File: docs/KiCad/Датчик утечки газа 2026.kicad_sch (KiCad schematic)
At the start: 30 parts, among them J1 Conn_01x04_Pin, J2 Conn_01x04_Pin, Q1 BC846BDW1, Q2 AO4807, U1 TGS_2611-E00, U2 LMR50410, U3 ATtiny412-SS

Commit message: Исправление разводки платы Ver_LIN
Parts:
- R2: footprint Resistor_SMD:R_1210_3225Metric_Pad1.30x2.65mm_HandSolder -> Resistor_SMD:R_1206_3216Metric
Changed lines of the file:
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@@
 			)
 		)
-		(property "Footprint" "Resistor_SMD:R_1210_3225Metric_Pad1.30x2.65mm_HandSolder"
+		(property "Footprint" "Resistor_SMD:R_1206_3216Metric"
 			(at 66.04 127.762 90)
 			(hide yes)

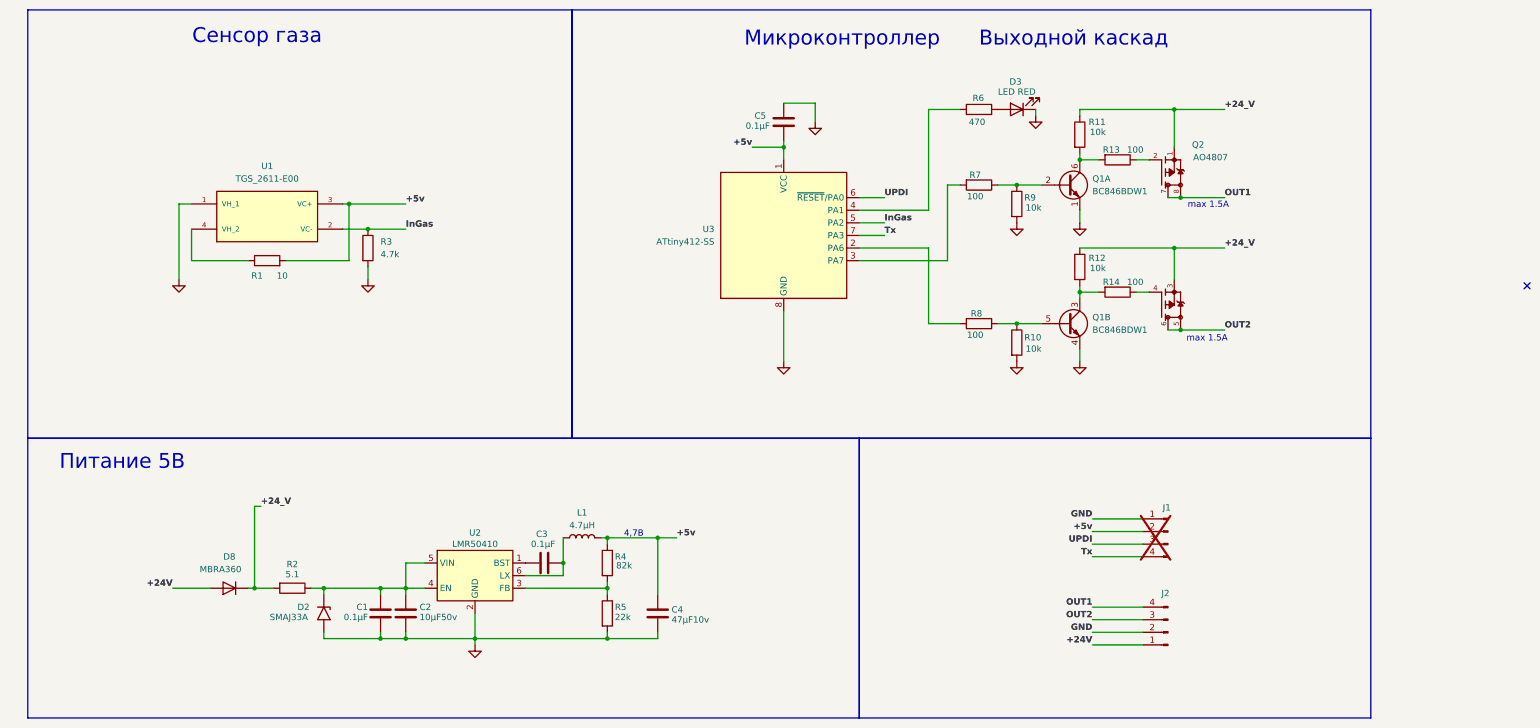
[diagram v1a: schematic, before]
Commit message: Изменить выходной ключ на умный. Правки печатной платы
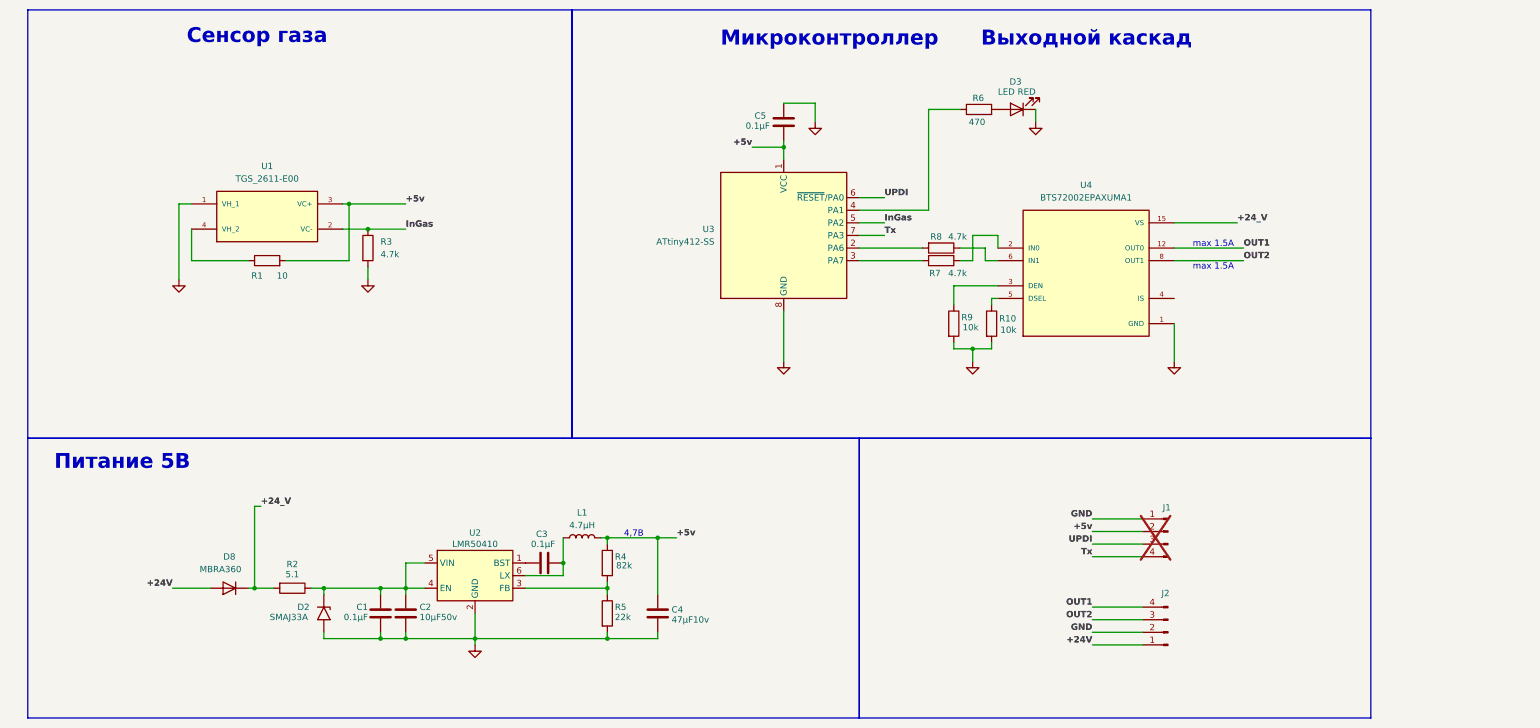
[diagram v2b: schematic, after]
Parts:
- removed Q1: BC846BDW1, Package_TO_SOT_SMD:SOT-363_SC-70-6, symbol Transistor_BJT:BC846BDW1
- removed Q2: AO4807, Package_SO:SOIC-8_3.9x4.9mm_P1.27mm, symbol AO4407A:AO4807
- removed R11, R12: 10k, Resistor_SMD:R_0603_1608Metric, symbol Device:R
- removed R13, R14: 100, Resistor_SMD:R_0603_1608Metric, symbol Device:R
- added U4: BTS72002EPAXUMA1, Package_TO_SOT_SMD:SOP65P600X115-15N_BTS72002EPAXUMA1, symbol Driver:BTS72002EPAXUMA1
- J2: footprint Connector_Pin:AMP SEAL 3.00mm_4p -> Connector_DIN:SSEAL_4
- R7, R8: value 100 -> 4.7k
- U1: footprint Sensor:TO180P920X780-4P -> Sensor_Humidity:TO180P920X780-4P
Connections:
- net +24_V: now also U4.15 (VS)
- net GND: now also U4.1 (GND)
- net OUT1: now also U4.12 (OUT0), U4.13 (OUT0), U4.14 (OUT0)
- net OUT2: now also U4.10 (OUT1), U4.8 (OUT1), U4.9 (OUT1)
- net at R7.1: now also U4.2 (IN0); no longer R9.1
- net at R10.1: now also U4.5 (DSEL); no longer R8.1
- new net: R9.1, U4.3 (DEN)
- new net: R8.1, U4.6 (IN1)
- no-connect marks 1 -> 0
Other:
- moved on the sheet: R10, R7, R8, R9

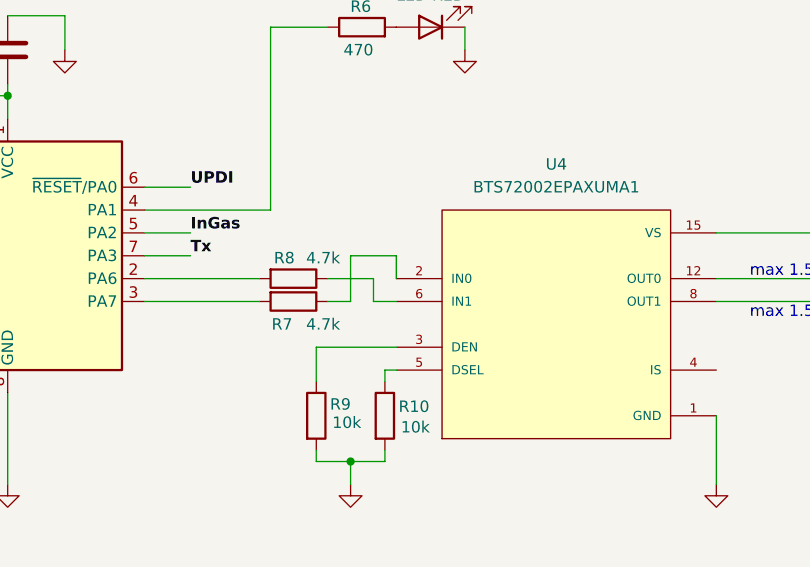
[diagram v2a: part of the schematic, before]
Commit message: Коррекция ПП. Замена выходной ключ на BTS72002
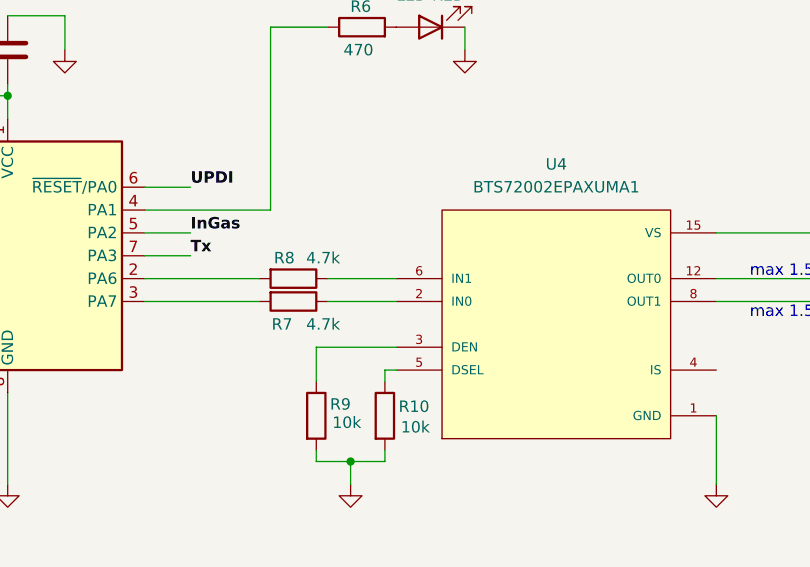
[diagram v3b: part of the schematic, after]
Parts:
- R2: footprint Resistor_SMD:R_1206_3216Metric -> Resistor_SMD:R_0805_2012Metric
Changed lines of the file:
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@@
 	(wire
 		(pts
-			(xy 208.28 58.42) (xy 208.28 60.96)
-		)
-		(stroke
-			(width 0)
-			(type default)
-		)
-	)
-	(wire
-		(pts
 			(xy 165.1 31.75) (xy 171.45 31.75)
 		)
@@
 	(wire
 		(pts
-			(xy 203.2 63.5) (xy 203.2 58.42)
-		)
-		(stroke
-			(width 0)
-			(type default)
-		)
-	)
-	(wire
-		(pts
 			(xy 207.01 71.12) (xy 208.28 71.12)
 		)
@@
 	(wire
 		(pts
-			(xy 205.74 63.5) (xy 208.28 63.5)
-		)
-		(stroke
-			(width 0)
-			(type default)
-		)
-	)
-	(wire
-		(pts
 			(xy 77.47 52.07) (xy 77.47 63.5)
 		)
@@
 	(wire
 		(pts
-			(xy 200.66 60.96) (xy 205.74 60.96)
+			(xy 200.66 60.96) (xy 208.28 60.96)
 		)
 		(stroke
@@
 	(wire
 		(pts
-			(xy 200.66 63.5) (xy 203.2 63.5)
+			(xy 200.66 63.5) (xy 208.28 63.5)
 		)
 		(stroke
@@
 	(wire
 		(pts
-			(xy 205.74 60.96) (xy 205.74 63.5)
-		)
-		(stroke
-			(width 0)
-			(type default)
-		)
-	)
-	(wire
-		(pts
 			(xy 227.33 135.89) (xy 237.49 135.89)
 		)
@@
 	(wire
 		(pts
-			(xy 203.2 58.42) (xy 208.28 58.42)
-		)
-		(stroke
-			(width 0)
-			(type default)
-		)
-	)
-	(wire
-		(pts
 			(xy 120.65 119.38) (xy 120.65 124.46)
 		)
@@
 			)
 		)
-		(property "Description" "AC0603KRX7R9BB104"
+		(property "Description" "Unpolarized capacitor"
 			(at 116.84 124.46 0)
 			(hide yes)
@@
 			)
 		)
-		(property "Description" "GRM21BR61A476ME15L"
+		(property "Description" "Unpolarized capacitor"
 			(at 139.7 134.62 0)
 			(hide yes)
@@
 			)
 		)
-		(property "Sim.Device" "MBRA360, Диод Шоттки 60В 3А [SMA / DO-214AC]"
+		(property "Sim.Device" "D"
 			(at 53.34 129.54 0)
 			(hide yes)
@@
 			)
 		)
-		(property "Description" "LQH44PN4R7MP0L"
+		(property "Description" "Inductor"
 			(at 124.46 119.38 0)
 			(hide yes)
@@
 			)
 		)
-		(property "Description" "FYLS-0805URC"
+		(property "Description" "Light emitting diode"
 			(at 212.09 33.02 0)
 			(hide yes)
@@
 			)
 		)
-		(property "Footprint" "Resistor_SMD:R_1206_3216Metric"
+		(property "Footprint" "Resistor_SMD:R_0805_2012Metric"
 			(at 66.04 127.762 90)
 			(hide yes)
@@
 			)
 		)
-		(property "Description" "AC0603KRX7R9BB104"
+		(property "Description" "Unpolarized capacitor"
 			(at 83.82 134.62 0)
 			(hide yes)
@@
 			)
 		)
-		(property "Description" "GRM21BR61H106KE43L"
+		(property "Description" "Unpolarized capacitor"
 			(at 88.9 134.62 0)
 			(hide yes)
@@
 			)
 		)
-		(property "Description" "AC0603KRX7R9BB104"
+		(property "Description" "Unpolarized capacitor"
 			(at 165.1 35.56 0)
 			(hide yes)

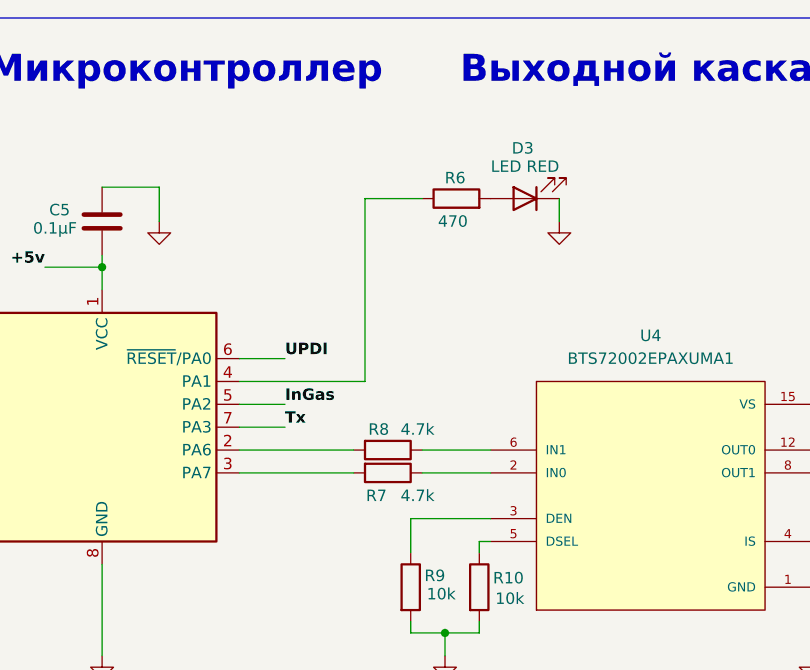
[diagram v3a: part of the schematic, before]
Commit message: Коррекция схемы для драйвера BTS72002EPAXUMA1
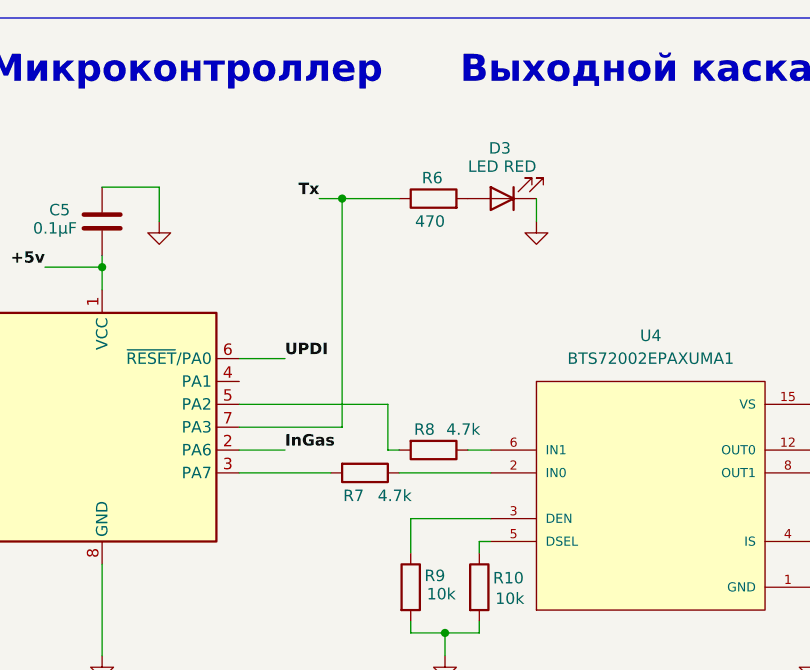
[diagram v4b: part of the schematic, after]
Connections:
- net InGas: now also U3.2 (PA6); no longer U3.5 (PA2)
- net Tx: now also R6.1
- net at R8.2: now also U3.5 (PA2); no longer U3.2 (PA6)
- net at U3.4 (PA1): no longer R6.1
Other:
- moved on the sheet: D3, R6, R7, R8
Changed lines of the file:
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@@
 	)
 	(junction
+		(at 191.77 33.02)
+		(diameter 0)
+		(color 0 0 0 0)
+	)
+	(junction
 		(at 83.82 139.7)
 		(diameter 0)
@@
 	(wire
 		(pts
-			(xy 194.31 33.02) (xy 200.66 33.02)
+			(xy 191.77 33.02) (xy 198.12 33.02)
 		)
 		(stroke
@@
 	(wire
 		(pts
-			(xy 180.34 55.88) (xy 185.42 55.88)
-		)
-		(stroke
-			(width 0)
-			(type default)
-		)
-	)
-	(wire
-		(pts
 			(xy 203.2 83.82) (xy 203.2 81.28)
 		)
@@
 	(wire
 		(pts
-			(xy 200.66 60.96) (xy 208.28 60.96)
+			(xy 205.74 60.96) (xy 208.28 60.96)
 		)
 		(stroke
@@
 	(wire
 		(pts
+			(xy 196.85 55.88) (xy 180.34 55.88)
+		)
+		(stroke
+			(width 0)
+			(type default)
+		)
+	)
+	(wire
+		(pts
 			(xy 207.01 72.39) (xy 207.01 71.12)
 		)
@@
 	(wire
 		(pts
-			(xy 200.66 63.5) (xy 208.28 63.5)
+			(xy 198.12 63.5) (xy 208.28 63.5)
 		)
 		(stroke
@@
 	(wire
 		(pts
-			(xy 180.34 58.42) (xy 185.42 58.42)
-		)
-		(stroke
-			(width 0)
-			(type default)
-		)
-	)
-	(wire
-		(pts
 			(xy 199.39 68.58) (xy 208.28 68.58)
 		)
@@
 	(wire
 		(pts
-			(xy 180.34 63.5) (xy 193.04 63.5)
+			(xy 180.34 63.5) (xy 190.5 63.5)
 		)
 		(stroke
@@
 	(wire
 		(pts
-			(xy 215.9 35.56) (xy 215.9 33.02)
+			(xy 213.36 35.56) (xy 213.36 33.02)
 		)
 		(stroke
@@
 	(wire
 		(pts
-			(xy 194.31 33.02) (xy 194.31 53.34)
+			(xy 180.34 58.42) (xy 191.77 58.42)
 		)
 		(stroke
@@
 	(wire
 		(pts
-			(xy 180.34 60.96) (xy 193.04 60.96)
+			(xy 191.77 33.02) (xy 191.77 58.42)
 		)
 		(stroke
@@
 	(wire
 		(pts
+			(xy 189.23 33.02) (xy 191.77 33.02)
+		)
+		(stroke
+			(width 0)
+			(type default)
+		)
+	)
+	(wire
+		(pts
 			(xy 207.01 81.28) (xy 207.01 80.01)
 		)
@@
 	(wire
 		(pts
+			(xy 196.85 60.96) (xy 196.85 55.88)
+		)
+		(stroke
+			(width 0)
+			(type default)
+		)
+	)
+	(wire
+		(pts
 			(xy 58.42 113.03) (xy 58.42 129.54)
 		)
@@
 	(wire
 		(pts
+			(xy 198.12 60.96) (xy 196.85 60.96)
+		)
+		(stroke
+			(width 0)
+			(type default)
+		)
+	)
+	(wire
+		(pts
 			(xy 64.77 63.5) (xy 77.47 63.5)
 		)
@@
 	(wire
 		(pts
-			(xy 81.28 67.31) (xy 81.28 64.77)
+			(xy 180.34 60.96) (xy 185.42 60.96)
 		)
 		(stroke
@@
 	(wire
 		(pts
-			(xy 129.54 139.7) (xy 129.54 138.43)
+			(xy 81.28 67.31) (xy 81.28 64.77)
 		)
 		(stroke
@@
 	(wire
 		(pts
-			(xy 57.15 129.54) (xy 58.42 129.54)
+			(xy 129.54 139.7) (xy 129.54 138.43)
 		)
 		(stroke
@@
 	(wire
 		(pts
-			(xy 77.47 52.07) (xy 88.9 52.07)
+			(xy 57.15 129.54) (xy 58.42 129.54)
 		)
 		(stroke
@@
 	(wire
 		(pts
-			(xy 194.31 53.34) (xy 180.34 53.34)
+			(xy 77.47 52.07) (xy 88.9 52.07)
 		)
 		(stroke
@@
 	)
 	(label "Tx"
-		(at 185.42 58.42 0)
-		(effects
-			(font
-				(size 1.27 1.27)
-				(thickness 0.254)
-				(bold yes)
-			)
-			(justify left bottom)
-		)
-	)
-	(label "Tx"
 		(at 227.33 123.19 180)
 		(effects
@@
 	)
 	(label "InGas"
-		(at 185.42 55.88 0)
+		(at 88.9 57.15 0)
 		(effects
 			(font
@@
 	)
 	(label "InGas"
-		(at 88.9 57.15 0)
+		(at 185.42 60.96 0)
 		(effects
 			(font
@@
 		)
 	)
+	(label "Tx"
+		(at 189.23 33.02 180)
+		(effects
+			(font
+				(size 1.27 1.27)
+				(thickness 0.254)
+				(bold yes)
+			)
+			(justify right bottom)
+		)
+	)
 	(label "OUT1"
 		(at 227.33 133.35 180)
@@
 	(symbol
 		(lib_id "Device:R")
-		(at 196.85 63.5 270)
+		(at 194.31 63.5 270)
 		(unit 1)
 		(body_style 1)
@@
 		(dnp no)
 		(property "Reference" "R7"
-			(at 195.58 66.04 90)
+			(at 193.04 66.04 90)
 			(show_name no)
 			(do_not_autoplace no)
@@
 		)
 		(property "Value" "4.7k"
-			(at 200.152 66.04 90)
+			(at 197.612 66.04 90)
 			(show_name no)
 			(do_not_autoplace no)
@@
 		)
 		(property "Footprint" "Resistor_SMD:R_0603_1608Metric"
-			(at 196.85 61.722 90)
+			(at 194.31 61.722 90)
 			(hide yes)
 			(show_name no)
@@
 		)
 		(property "Datasheet" ""
-			(at 196.85 63.5 0)
+			(at 194.31 63.5 0)
 			(hide yes)
 			(show_name no)
@@
 		)
 		(property "Description" "Resistor"
-			(at 196.85 63.5 0)
+			(at 194.31 63.5 0)
 			(hide yes)
 			(show_name no)
@@
 	(symbol
 		(lib_id "power:GND")
-		(at 215.9 35.56 0)
+		(at 213.36 35.56 0)
 		(unit 1)
 		(body_style 1)
@@
 		(fields_autoplaced yes)
 		(property "Reference" "#PWR08"
-			(at 215.9 41.91 0)
+			(at 213.36 41.91 0)
 			(hide yes)
 			(show_name no)
@@
 		)
 		(property "Value" "GND"
-			(at 215.9 40.64 0)
+			(at 213.36 40.64 0)
 			(hide yes)
 			(show_name no)
@@
 		)
 		(property "Footprint" ""
-			(at 215.9 35.56 0)
+			(at 213.36 35.56 0)
 			(hide yes)
 			(show_name no)
@@
 		)
 		(property "Datasheet" ""
-			(at 215.9 35.56 0)
+			(at 213.36 35.56 0)
 			(hide yes)
 			(show_name no)
@@
 		)
 		(property "Description" "Power symbol creates a global label with name \"GND\" , ground"
-			(at 215.9 35.56 0)
+			(at 213.36 35.56 0)
 			(hide yes)
 			(show_name no)
@@
 	(symbol
 		(lib_id "Device:LED")
-		(at 212.09 33.02 180)
+		(at 209.55 33.02 180)
 		(unit 1)
 		(body_style 1)
@@
 		(dnp no)
 		(property "Reference" "D3"
-			(at 211.836 27.432 0)
+			(at 209.296 27.432 0)
 			(show_name no)
 			(do_not_autoplace no)
@@
 		)
 		(property "Value" "LED RED"
-			(at 212.09 29.464 0)
+			(at 209.55 29.464 0)
 			(show_name no)
 			(do_not_autoplace no)
@@
 		)
 		(property "Footprint" "LED_SMD:LED_0805_2012Metric"
-			(at 212.09 33.02 0)
+			(at 209.55 33.02 0)
 			(hide yes)
 			(show_name no)
@@
 		)
 		(property "Datasheet" ""
-			(at 212.09 33.02 0)
+			(at 209.55 33.02 0)
 			(hide yes)
 			(show_name no)
@@
 		)
 		(property "Description" "Light emitting diode"
-			(at 212.09 33.02 0)
+			(at 209.55 33.02 0)
 			(hide yes)
 			(show_name no)
@@
 		)
 		(property "Sim.Pins" "1=K 2=A"
-			(at 212.09 33.02 0)
+			(at 209.55 33.02 0)
 			(hide yes)
 			(show_name no)
@@
 	(symbol
 		(lib_id "Device:R")
-		(at 196.85 60.96 270)
+		(at 201.93 60.96 270)
 		(unit 1)
 		(body_style 1)
@@
 		(dnp no)
 		(property "Reference" "R8"
-			(at 195.834 58.674 90)
+			(at 200.914 58.674 90)
 			(show_name no)
 			(do_not_autoplace no)
@@
 		)
 		(property "Value" "4.7k"
-			(at 200.152 58.674 90)
+			(at 205.232 58.674 90)
 			(show_name no)
 			(do_not_autoplace no)
@@
 		)
 		(property "Footprint" "Resistor_SMD:R_0603_1608Metric"
-			(at 196.85 59.182 90)
+			(at 201.93 59.182 90)
 			(hide yes)
 			(show_name no)
@@
 		)
 		(property "Datasheet" ""
-			(at 196.85 60.96 0)
+			(at 201.93 60.96 0)
 			(hide yes)
 			(show_name no)
@@
 		)
 		(property "Description" "Resistor"
-			(at 196.85 60.96 0)
+			(at 201.93 60.96 0)
 			(hide yes)
 			(show_name no)
@@
 	(symbol
 		(lib_id "Device:R")
-		(at 204.47 33.02 90)
+		(at 201.93 33.02 90)
 		(unit 1)
 		(body_style 1)
@@
 		(dnp no)
 		(property "Reference" "R6"
-			(at 205.486 30.734 90)
+			(at 202.946 30.734 90)
 			(show_name no)
 			(do_not_autoplace no)
@@
 		)
 		(property "Value" "470"
-			(at 205.74 35.56 90)
+			(at 203.2 35.56 90)
 			(show_name no)
 			(do_not_autoplace no)
@@
 		)
 		(property "Footprint" "Resistor_SMD:R_0603_1608Metric"
-			(at 204.47 34.798 90)
+			(at 201.93 34.798 90)
 			(hide yes)
 			(show_name no)
@@
 		)
 		(property "Datasheet" ""
-			(at 204.47 33.02 0)
+			(at 201.93 33.02 0)
 			(hide yes)
 			(show_name no)
@@
 		)
 		(property "Description" "Resistor"
-			(at 204.47 33.02 0)
+			(at 201.93 33.02 0)
 			(hide yes)
 			(show_name no)
